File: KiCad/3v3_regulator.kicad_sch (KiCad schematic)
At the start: 14 parts, among them U2 LMR36006BRNXT

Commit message: new layout
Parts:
- NT6: footprint (none) -> NetTie:NetTie-2_SMD_Pad0.5mm
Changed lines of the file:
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@@
 			)
 		)
-		(property "Footprint" ""
+		(property "Footprint" "NetTie:NetTie-2_SMD_Pad0.5mm"
 			(at 115.57 101.6 0)
 			(effects

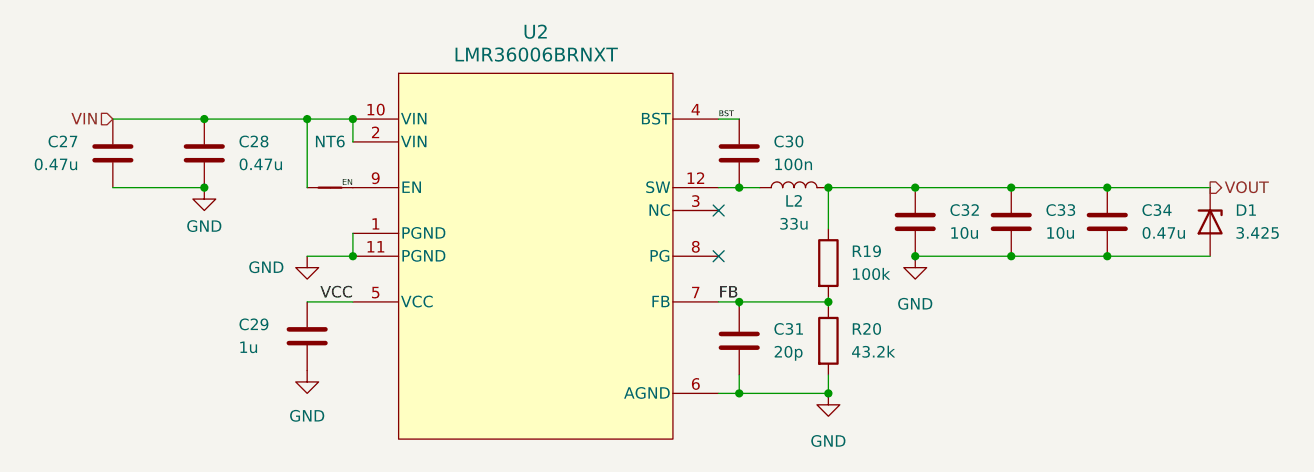
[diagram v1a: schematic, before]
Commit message: standalone regulator core
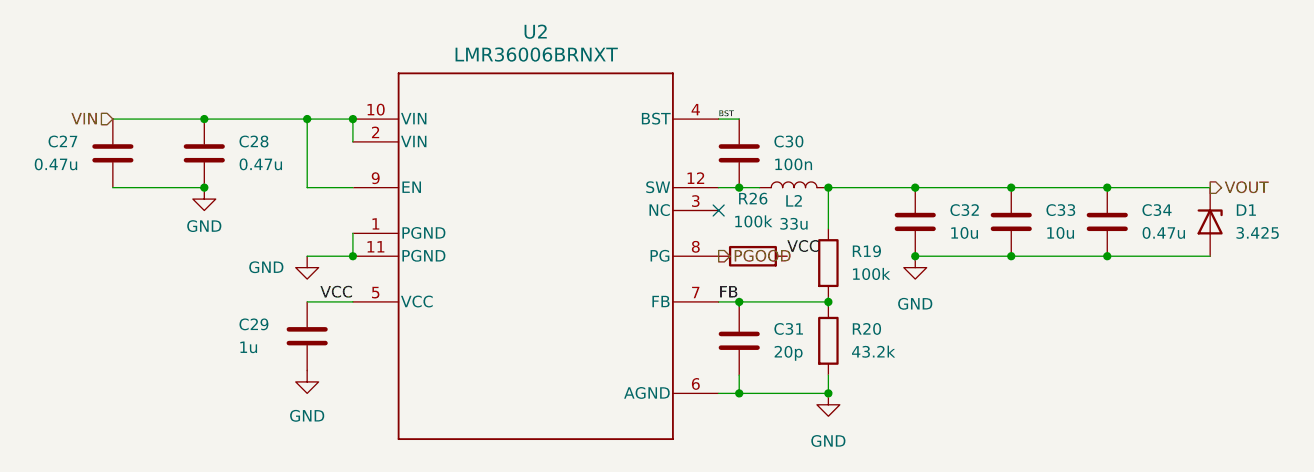
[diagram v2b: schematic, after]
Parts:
- removed NT6: NetTie_2, NetTie:NetTie-2_SMD_Pad0.5mm, symbol Device:NetTie_2
- added R26: 100k, Resistor_SMD:R_0603_1608Metric, symbol Device:R
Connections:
- net EN is gone; now on net VIN: U2.9 (EN)
- net VCC: now also R26.2
- net PGOOD: now reaches U2.8 (PG)
- net PGOOD: now also R26.1
- no-connect marks 2 -> 1
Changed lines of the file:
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@@
 		(at 158.75 104.14)
 	)
-	(no_connect
-		(at 158.75 109.22)
-	)
 	(wire
 		(pts
@@
 		(pts
 			(xy 91.44 101.6) (xy 101.6 101.6)
+		)
+		(stroke
+			(width 0)
+			(type default)
+		)
+	)
+	(wire
+		(pts
+			(xy 113.03 101.6) (xy 118.11 101.6)
 		)
 		(stroke
@@
 		)
 	)
-	(label "EN"
-		(at 118.11 101.6 180)
+	(label "VCC"
+		(at 166.37 109.22 0)
+		(fields_autoplaced yes)
+		(effects
+			(font
+				(size 1.27 1.27)
+			)
+			(justify left bottom)
+		)
+	)
+	(label "BST"
+		(at 158.75 93.98 0)
 		(fields_autoplaced yes)
 		(effects
@@
 				(size 0.635 0.635)
 			)
-			(justify right bottom)
-		)
-	)
-	(label "BST"
-		(at 158.75 93.98 0)
+			(justify left bottom)
+		)
+	)
+	(hierarchical_label "PGOOD"
+		(shape output)
+		(at 158.75 109.22 0)
 		(fields_autoplaced yes)
 		(effects
 			(font
-				(size 0.635 0.635)
-			)
-			(justify left bottom)
+				(size 1.27 1.27)
+			)
+			(justify left)
 		)
 	)
@@
 			)
 		)
-		(property "Description" ""
+		(property "Description" "Unpolarized capacitor"
 			(at 201.93 105.41 0)
 			(effects
@@
 			)
 		)
-		(property "Description" ""
+		(property "Description" "Power symbol creates a global label with name \"GND\" , ground"
 			(at 170.942 124.46 0)
 			(effects
@@
 			)
 		)
-		(property "Description" ""
+		(property "Description" "Resistor"
 			(at 170.942 109.982 0)
 			(effects
@@
 			)
 		)
-		(property "Datasheet" "https://www.ti.com/lit/ds/symlink/lmr36006.pdf"
+		(property "Datasheet" "LMR36006BRNXT"
 			(at 138.43 109.22 0)
 			(effects
@@
 			)
 		)
-		(property "Datasheet" "https://www.vishay.com/docs/84830/plzseries.pdf"
+		(property "Datasheet" "~"
 			(at 213.36 105.41 0)
 			(effects
@@
 			)
 		)
-		(property "Description" ""
+		(property "Description" "Zener diode"
 			(at 213.36 105.41 0)
 			(effects
@@
 			)
 		)
-		(property "Description" ""
+		(property "Description" "Unpolarized capacitor"
 			(at 101.6 97.79 0)
 			(effects
@@
 			)
 		)
-		(property "Description" ""
+		(property "Description" "Power symbol creates a global label with name \"GND\" , ground"
 			(at 101.6 101.6 0)
 			(effects
@@
 			)
 		)
-		(property "Description" ""
+		(property "Description" "Power symbol creates a global label with name \"GND\" , ground"
 			(at 113.03 109.22 0)
 			(effects
@@
 			)
 		)
-		(property "Description" ""
+		(property "Description" "Power symbol creates a global label with name \"GND\" , ground"
 			(at 180.594 109.22 0)
 			(effects
@@
 			)
 		)
-		(property "Description" ""
+		(property "Description" "Unpolarized capacitor"
 			(at 91.44 97.79 0)
 			(effects
@@
 			)
 		)
-		(property "Description" ""
+		(property "Description" "Resistor"
 			(at 170.942 118.618 0)
 			(effects
@@
 				(path "/2223e2d2-71c8-4f08-b970-c0182a3b98e5/ac916dc0-126e-4456-8ac4-6182257da33b"
 					(reference "R20")
-					(unit 1)
-				)
-			)
-		)
-	)
-	(symbol
-		(lib_id "Device:NetTie_2")
-		(at 115.57 101.6 0)
-		(unit 1)
-		(exclude_from_sim no)
-		(in_bom no)
-		(on_board yes)
-		(dnp no)
-		(fields_autoplaced yes)
-		(property "Reference" "NT6"
-			(at 115.57 96.52 0)
-			(effects
-				(font
-					(size 1.27 1.27)
-				)
-			)
-		)
-		(property "Value" "NetTie_2"
-			(at 115.57 99.06 0)
-			(effects
-				(font
-					(size 1.27 1.27)
-				)
-				(hide yes)
-			)
-		)
-		(property "Footprint" "NetTie:NetTie-2_SMD_Pad0.5mm"
-			(at 115.57 101.6 0)
-			(effects
-				(font
-					(size 1.27 1.27)
-				)
-				(hide yes)
-			)
-		)
-		(property "Datasheet" "~"
-			(at 115.57 101.6 0)
-			(effects
-				(font
-					(size 1.27 1.27)
-				)
-				(hide yes)
-			)
-		)
-		(property "Description" "Net tie, 2 pins"
-			(at 115.57 101.6 0)
-			(effects
-				(font
-					(size 1.27 1.27)
-				)
-				(hide yes)
-			)
-		)
-		(pin "1"
-		)
-		(pin "2"
-		)
-		(instances
-			(project ""
-				(path "/2223e2d2-71c8-4f08-b970-c0182a3b98e5/ac916dc0-126e-4456-8ac4-6182257da33b"
-					(reference "NT6")
 					(unit 1)
 				)
@@
 			)
 		)
-		(property "Description" ""
+		(property "Description" "Unpolarized capacitor"
 			(at 161.036 97.79 0)
 			(effects
@@
 			)
 		)
-		(property "Datasheet" "https://www.we-online.com/components/products/datasheet/74438335330.pdf"
+		(property "Datasheet" "~"
 			(at 167.132 101.6 0)
 			(effects
@@
 			)
 		)
-		(property "Description" ""
+		(property "Description" "Inductor"
 			(at 167.132 101.6 0)
 			(effects
@@
 			)
 		)
-		(property "Description" ""
+		(property "Description" "Power symbol creates a global label with name \"GND\" , ground"
 			(at 113.03 121.92 0)
 			(effects
@@
 			)
 		)
-		(property "Description" ""
+		(property "Description" "Unpolarized capacitor"
 			(at 180.594 105.41 0)
 			(effects
@@
 				(path "/2223e2d2-71c8-4f08-b970-c0182a3b98e5/ac916dc0-126e-4456-8ac4-6182257da33b"
 					(reference "C32")
+					(unit 1)
+				)
+			)
+		)
+	)
+	(symbol
+		(lib_id "Device:R")
+		(at 162.56 109.22 90)
+		(unit 1)
+		(exclude_from_sim no)
+		(in_bom yes)
+		(on_board yes)
+		(dnp no)
+		(fields_autoplaced yes)
+		(property "Reference" "R26"
+			(at 162.56 102.87 90)
+			(effects
+				(font
+					(size 1.27 1.27)
+				)
+			)
+		)
+		(property "Value" "100k"
+			(at 162.56 105.41 90)
+			(effects
+				(font
+					(size 1.27 1.27)
+				)
+			)
+		)
+		(property "Footprint" "Resistor_SMD:R_0603_1608Metric"
+			(at 162.56 110.998 90)
+			(effects
+				(font
+					(size 1.27 1.27)
+				)
+				(hide yes)
+			)
+		)
+		(property "Datasheet" "~"
+			(at 162.56 109.22 0)
+			(effects
+				(font
+					(size 1.27 1.27)
+				)
+				(hide yes)
+			)
+		)
+		(property "Description" "Resistor"
+			(at 162.56 109.22 0)
+			(effects
+				(font
+					(size 1.27 1.27)
+				)
+				(hide yes)
+			)
+		)
+		(pin "1"
+		)
+		(pin "2"
+		)
+		(instances
+			(project "PD Charger"
+				(path "/2223e2d2-71c8-4f08-b970-c0182a3b98e5/ac916dc0-126e-4456-8ac4-6182257da33b"
+					(reference "R26")
 					(unit 1)
 				)
@@
 			)
 		)
-		(property "Description" ""
+		(property "Description" "Unpolarized capacitor"
 			(at 191.262 105.41 0)
 			(effects
@@
 			)
 		)
-		(property "Description" ""
+		(property "Description" "Unpolarized capacitor"
 			(at 161.036 118.618 0)
 			(effects
@@
 			)
 		)
-		(property "Description" ""
+		(property "Description" "Unpolarized capacitor"
 			(at 113.03 118.11 0)
 			(effects
